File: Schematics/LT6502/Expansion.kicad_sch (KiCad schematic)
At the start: 8 parts, among them J9 DIN41612_02x32_AC

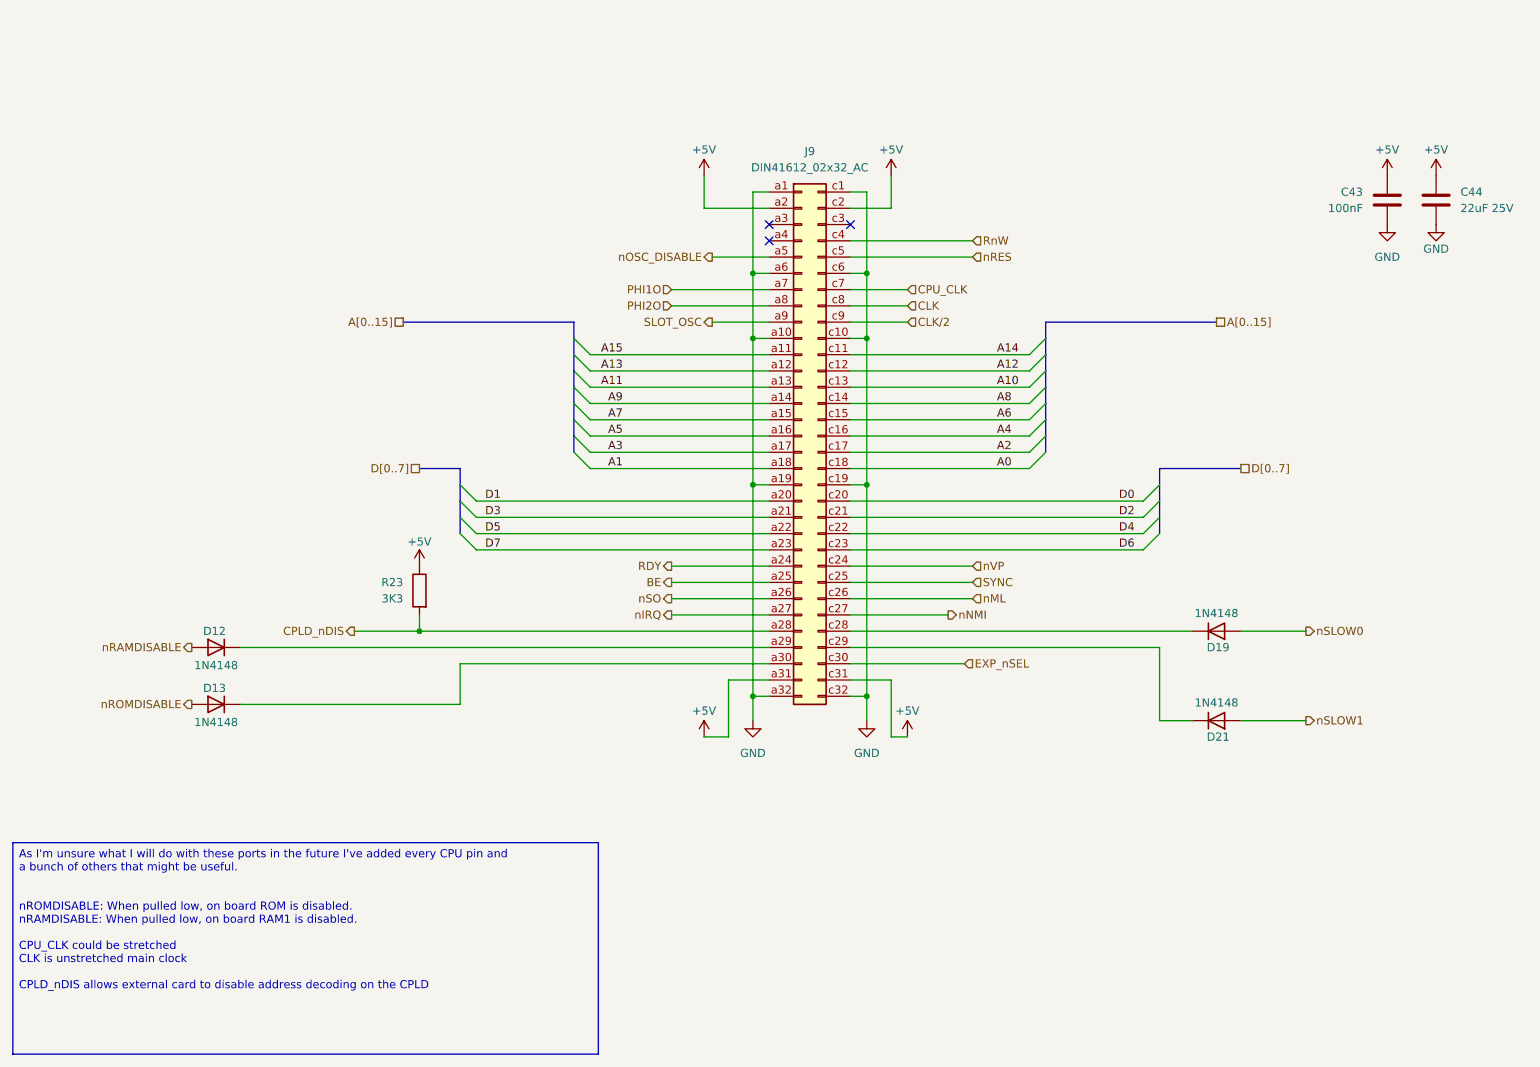
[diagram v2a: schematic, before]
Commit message: Updated BoMs ordered PCBs
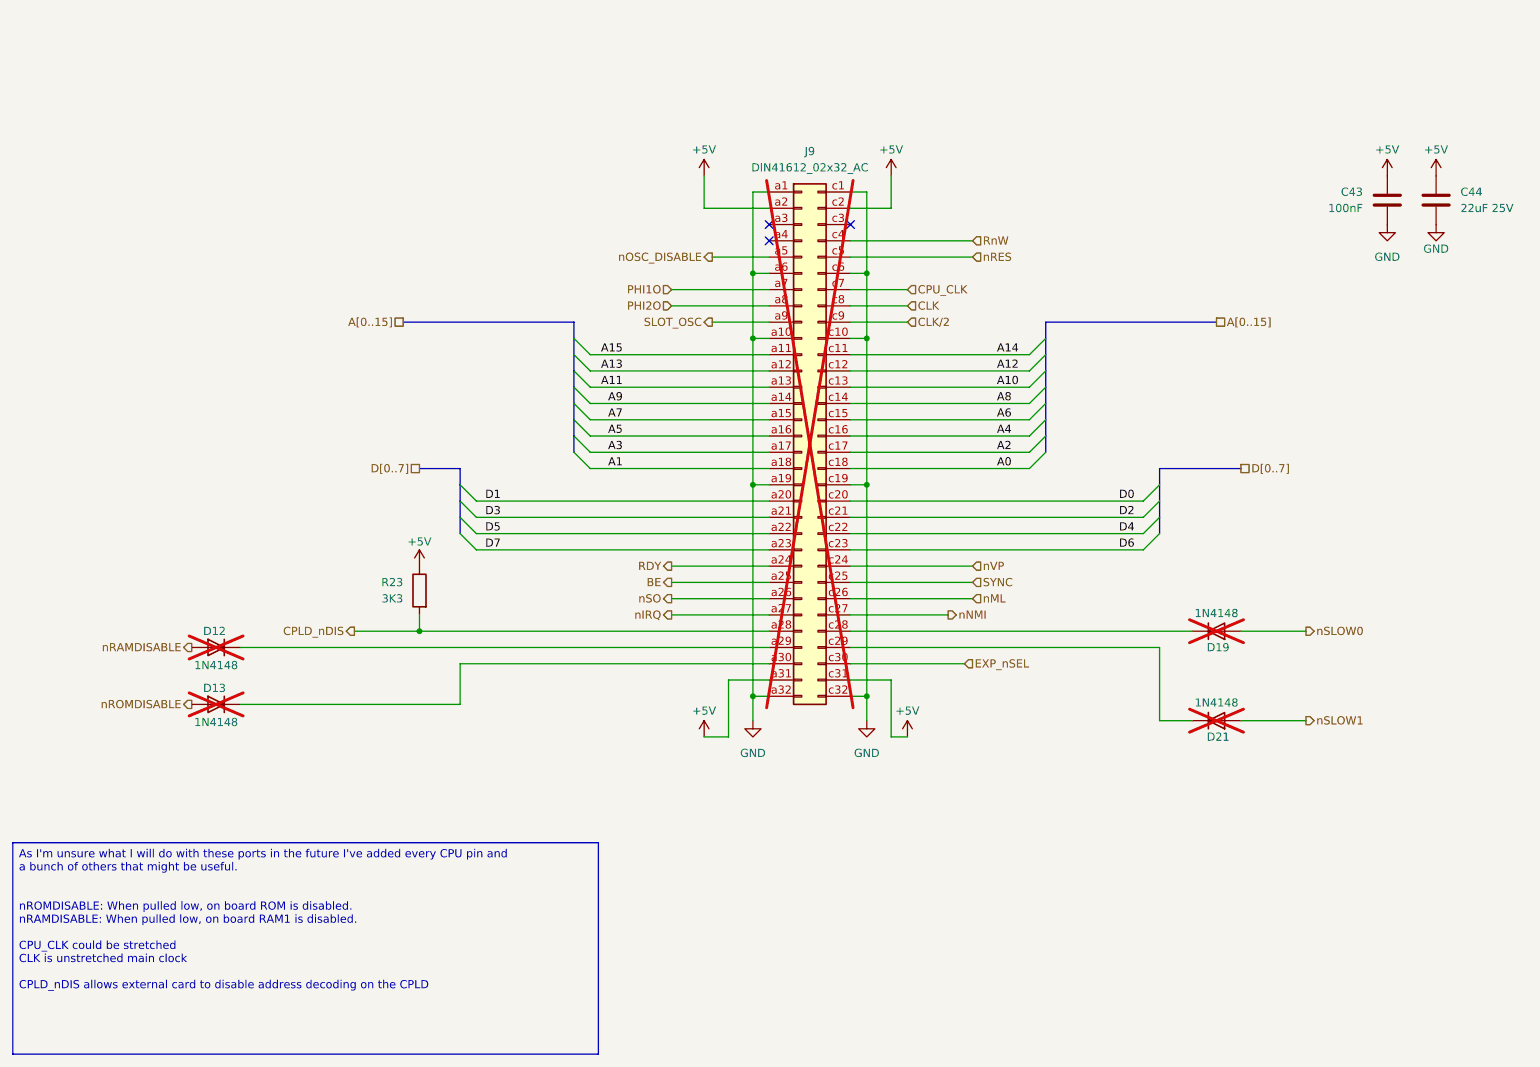
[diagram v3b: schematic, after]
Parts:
- C43: LCSC C49678 -> C113803
- C44: LCSC (none) -> C45783
- D12, D13, D19, D21, J9: LCSC (none) -> DNF; now not fitted
- R23: LCSC DNF -> C25890
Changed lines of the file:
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@@
+			)
+		)
+		(property "LCSC" "C45783"
+			(at 252.73 57.15 0)
+			(effects
+				(font
+					(size 1.27 1.27)
+				)
+				(hide yes)
 			)
 		)
@@
 		(in_bom yes)
 		(on_board yes)
-		(dnp no)
+		(dnp yes)
 		(property "Reference" "D12"
 			(at 61.976 124.46 0)
@@
 		)
 		(property "Sim.Pins" "1=K 2=A"
+			(at 62.23 127 0)
+			(effects
+				(font
+					(size 1.27 1.27)
+				)
+				(hide yes)
+			)
+		)
+		(property "LCSC" "DNF"
 			(at 62.23 127 0)
 			(effects
@@
 		(in_bom yes)
 		(on_board yes)
-		(dnp no)
+		(dnp yes)
 		(property "Reference" "D21"
 			(at 218.694 140.97 0)
@@
 			)
 		)
+		(property "LCSC" "DNF"
+			(at 218.44 138.43 0)
+			(effects
+				(font
+					(size 1.27 1.27)
+				)
+				(hide yes)
+			)
+		)
 		(pin "2"
 		)
@@
 		(in_bom yes)
 		(on_board yes)
-		(dnp no)
+		(dnp yes)
 		(fields_autoplaced yes)
 		(property "Reference" "J9"
@@
 		)
 		(property "Mouser Part Number" "649-864648813H55V1LF"
+			(at 153.67 93.98 0)
+			(effects
+				(font
+					(size 1.27 1.27)
+				)
+				(hide yes)
+			)
+		)
+		(property "LCSC" "DNF"
 			(at 153.67 93.98 0)
 			(effects
@@
 			)
 		)
-		(property "LCSC" "C49678"
+		(property "LCSC" "C113803"
 			(at 245.11 57.15 0)
 			(effects
@@
 		(in_bom yes)
 		(on_board yes)
-		(dnp no)
+		(dnp yes)
 		(property "Reference" "D19"
 			(at 218.694 127 0)
@@
 		)
 		(property "Sim.Pins" "1=K 2=A"
+			(at 218.44 124.46 0)
+			(effects
+				(font
+					(size 1.27 1.27)
+				)
+				(hide yes)
+			)
+		)
+		(property "LCSC" "DNF"
 			(at 218.44 124.46 0)
 			(effects
@@
 			)
 		)
-		(property "LCSC" "DNF"
+		(property "LCSC" "C25890"
 			(at 93.98 118.11 0)
 			(effects
@@
 		(in_bom yes)
 		(on_board yes)
-		(dnp no)
+		(dnp yes)
 		(property "Reference" "D13"
 			(at 61.976 133.35 0)
@@
 			(at 62.23 135.89 0)
 			(effects
+				(font
+					(size 1.27 1.27)
+				)
+				(hide yes)
+			)
+		)
+		(property "LCSC" "DNF"
+			(at 62.23 135.89 0)
+			(effects

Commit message: Auto stash before merge of "main" and "origin/main"
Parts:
- D12, D13, D19, D21, J9: now fitted
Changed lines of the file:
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@@
 		(in_bom yes)
 		(on_board yes)
-		(dnp yes)
+		(dnp no)
 		(property "Reference" "D12"
 			(at 61.976 124.46 0)
@@
 		(in_bom yes)
 		(on_board yes)
-		(dnp yes)
+		(dnp no)
 		(property "Reference" "D21"
 			(at 218.694 140.97 0)
@@
 		(in_bom yes)
 		(on_board yes)
-		(dnp yes)
+		(dnp no)
 		(fields_autoplaced yes)
 		(property "Reference" "J9"
@@
 		(in_bom yes)
 		(on_board yes)
-		(dnp yes)
+		(dnp no)
 		(property "Reference" "D19"
 			(at 218.694 127 0)
@@
 		(in_bom yes)
 		(on_board yes)
-		(dnp yes)
+		(dnp no)
 		(property "Reference" "D13"
 			(at 61.976 133.35 0)
